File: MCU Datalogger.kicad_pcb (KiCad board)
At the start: 2 copper layers, 29 parts, among them J1 Conn_01x04_Pin, J2 Conn_01x09_Pin, J3 Conn_01x04_Pin, J4 Conn_02x03_Odd_Even, U1 24LC1025, U2 DS1337S_, U3 24LC1025, U4 ATMEGA328P-AU, Y1 32.768 KHz, Y2 16 MHz

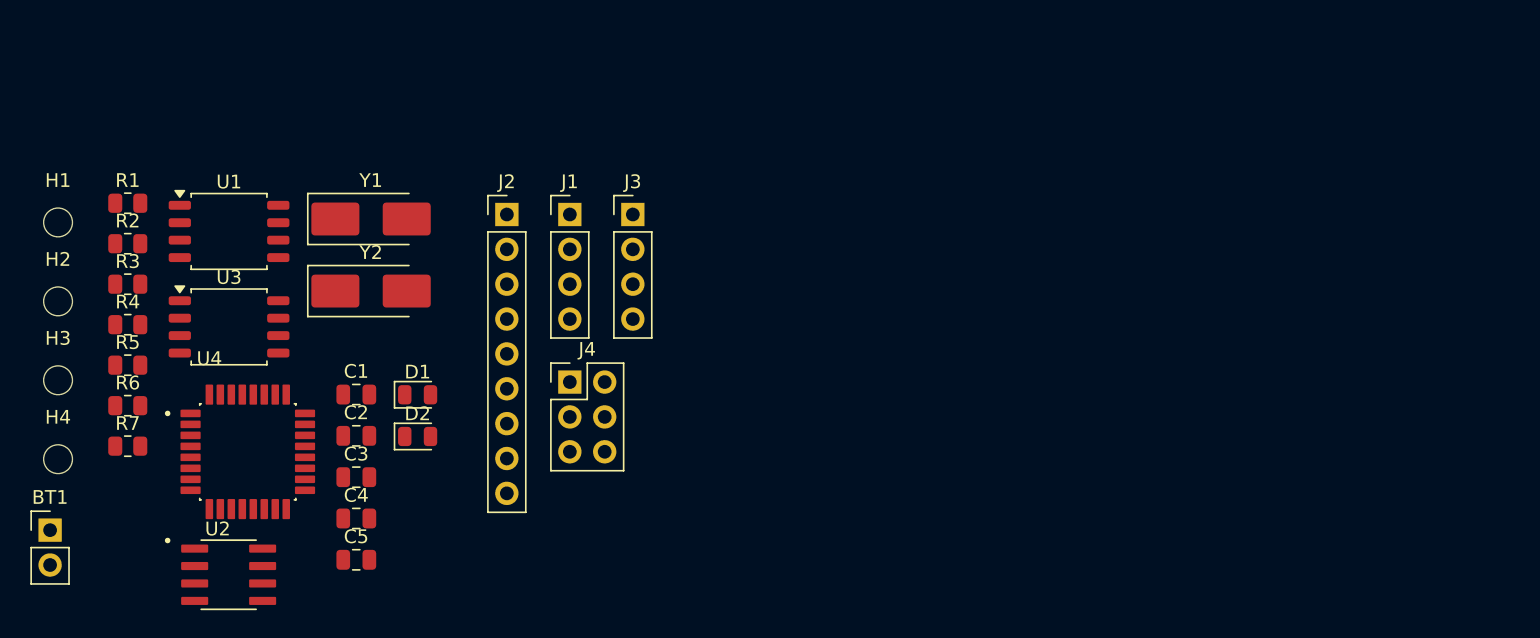
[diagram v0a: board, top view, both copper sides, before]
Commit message: completed placements of footprints
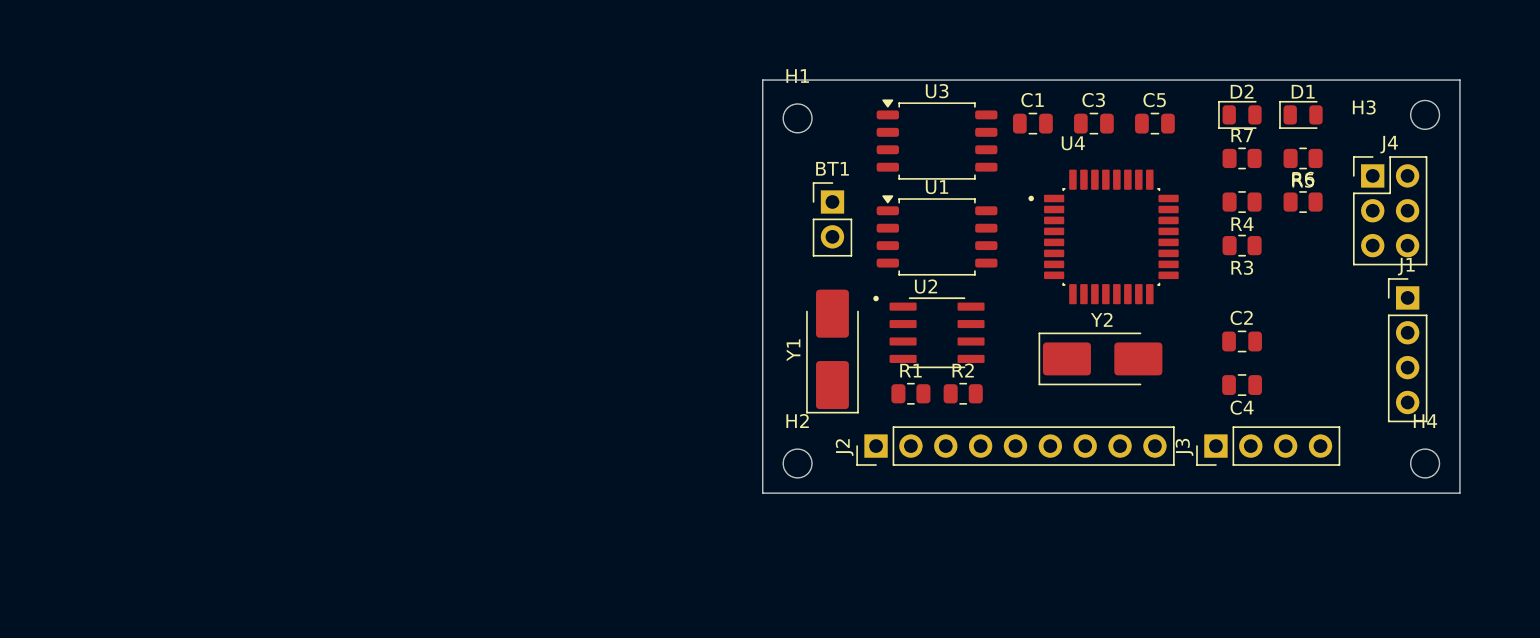
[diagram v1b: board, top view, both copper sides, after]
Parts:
- moved H3 101.5 mm to (213.4, 74.3)
- moved H4 99.6 mm to (213.4, 99.7)
- moved R5 87.0 mm to (204.5, 77.5), turned to 180 degrees
- moved R6 86.9 mm to (204.5, 80.6)
- moved R7 83.9 mm to (200.0, 77.5)
- moved R4 81.7 mm to (200.0, 80.6), turned to 180 degrees
- moved R3 81.2 mm to (200.0, 83.8), turned to 180 degrees
- moved D1 67.7 mm to (204.5, 74.3)
- moved C5 66.3 mm to (193.7, 74.9)
- moved C4 65.3 mm to (200.0, 94.0), turned to 180 degrees
- moved C2 64.9 mm to (200.0, 90.8)
- moved U4 64.8 mm to (190.5, 83.2)
- moved D2 64.5 mm to (200.0, 74.3)
- moved R2 61.8 mm to (179.7, 94.6)
- moved BT1 61.8 mm to (170.2, 80.6)
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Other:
- board outline added: 50.8 x 30.1 mm

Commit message: finished tracks
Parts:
- moved H1 3.78 mm to (165.1, 71.8)
- moved H3 3.59 mm to (215.9, 71.8)
- moved H2 2.84 mm to (165.1, 101.0)
- moved H4 2.84 mm to (215.9, 101.0)
- turned Y2 to 180 degrees
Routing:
- net /VCC: track 0.00 -> 146.3 mm, vias 0 -> 2
- net /SCK: track 0.00 -> 111.9 mm, vias 0 -> 1
- net GND: track 0.00 -> 67.0 mm, vias 0 -> 6
- net /SDA: track 0.00 -> 62.5 mm, vias 0 -> 4
- net Net-(BT1-+): track 0.00 -> 46.3 mm, vias 0 -> 2
- net Net-(U4-PB7): track 0.00 -> 39.8 mm, vias 0 -> 4
- net /MOSI: track 0.00 -> 32.7 mm, vias 0 -> 1
- net /TX: track 0.00 -> 32.2 mm, vias 0 -> 1
- net /RX: track 0.00 -> 26.7 mm, vias 0 -> 1
- net /RESET: track 0.00 -> 26.1 mm, vias 0 -> 2
- net /D2: track 0.00 -> 25.4 mm, vias 0 -> 1
- net /MISO: track 0.00 -> 25.3 mm, vias 0 -> 1
- net /D3: track 0.00 -> 25.3 mm
- net Net-(U4-PB6): track 0.00 -> 22.6 mm
- net /D4: track 0.00 -> 22.2 mm
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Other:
- board size 50.8 x 30.1 mm -> 58.4 x 36.8 mm

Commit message: finished copper fields
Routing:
- net GND: track 67.0 -> 116.2 mm, vias 6 -> 10
- net Net-(BT1-+): track 46.3 -> 53.5 mm, vias 2 -> 3
- net /TX: track 32.2 -> 36.0 mm, vias 1 -> 2
- net /VCC: track 146.3 -> 148.3 mm
- net /D5: track 21.2 -> 19.5 mm
- net /SDA: track 62.5 -> 63.3 mm
- net /D2: track 25.4 -> 26.2 mm
- net /RESET: track 26.1 -> 26.6 mm
- added copper zone on F.Cu, net /VCC
- added copper zone on B.Cu, net GND

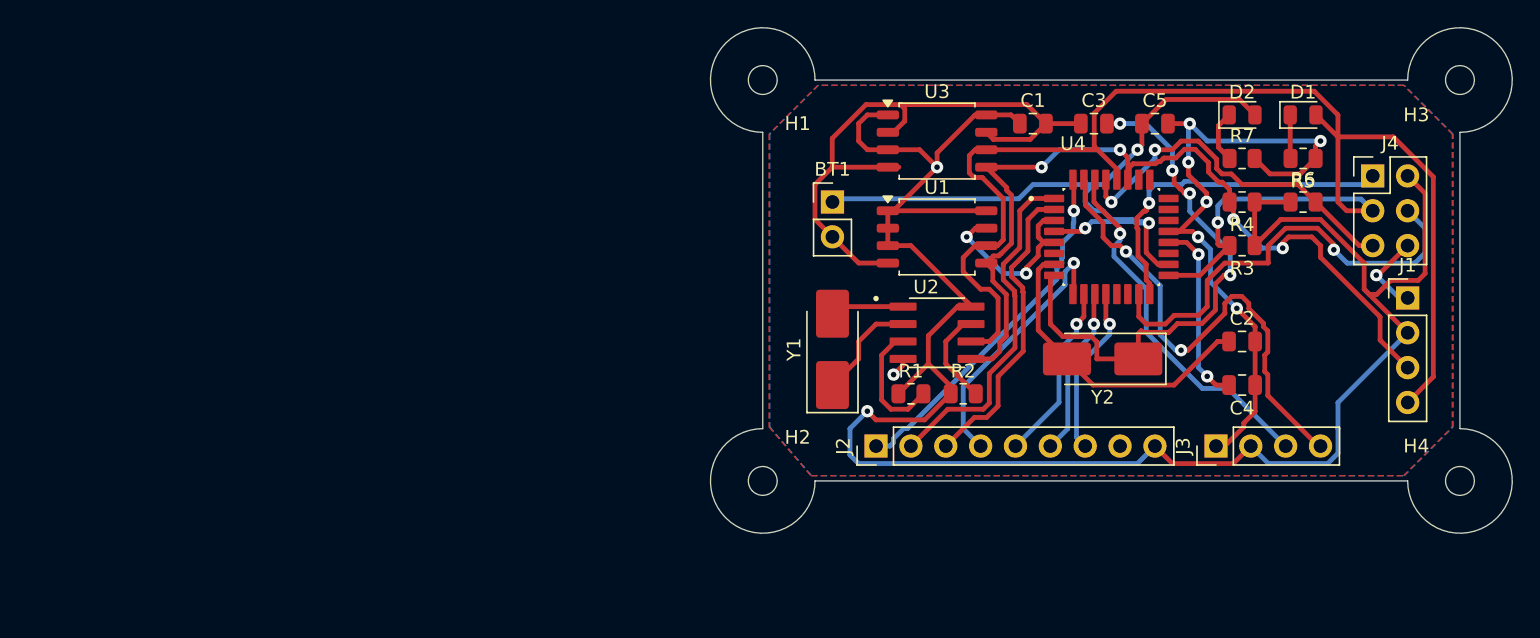
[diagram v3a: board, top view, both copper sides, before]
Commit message: finished silkscreen
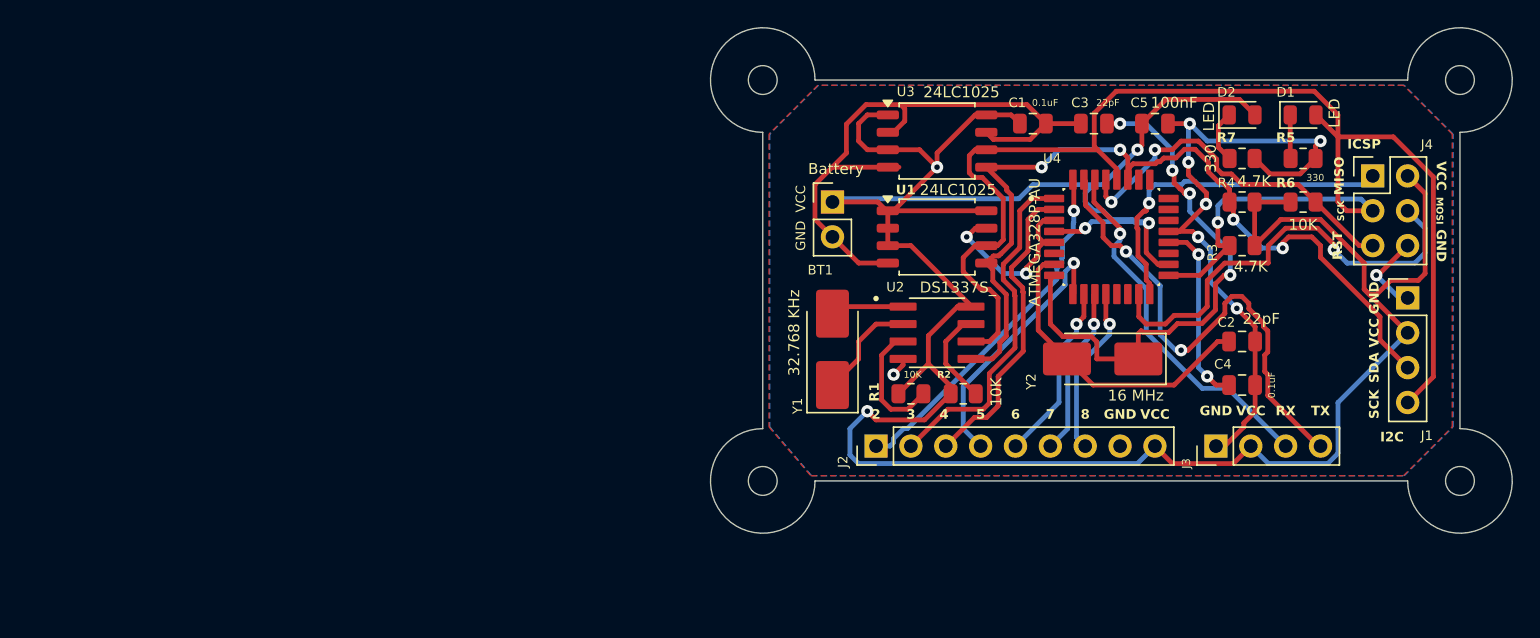
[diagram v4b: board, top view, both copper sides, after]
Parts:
- added REF**: KiCad-Logo2_5mm_SilkScreen, Symbol:KiCad-Logo2_5mm_SilkScreen, B.Cu at (190.0, 77.2)
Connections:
- BT1 pad 1: Net-(BT1-+) -> /VCC
- C5 pad 1: Net-(BT1-+) -> /VCC
- D2 pad 2: Net-(BT1-+) -> /VCC
- U4 pad 18: Net-(BT1-+) -> /VCC
- U4 pad 4: Net-(BT1-+) -> /VCC
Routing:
- net /VCC: track 148.3 -> 206.1 mm, vias 2 -> 5
- net Net-(BT1-+): track 53.5 -> 0.00 mm, vias 3 -> 0
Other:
- board text added: "2"
- board text added: "3"
- board text added: "4"
- board text added: "5"
- board text added: "6"
- board text added: "7"
- board text added: "8"
- board text added: "Data logger with ATMEGA328P"
- board text added: "Designed by Nisham Parakkal"
- board text added: "GND"
- board text added: "I2C"
- board text added: "ICSP"
- board text added: "MISO"
- board text added: "MOSI"
- board text added: "RST"
- board text added: "RX"
- board text added: "SCK"
- board text added: "SDA"
- board text added: "TX"
- board text added: "VCC"
